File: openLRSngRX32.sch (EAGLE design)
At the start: 50 parts, among them IC1 STM32F10XCXT6, IC2 REG1117, U1 MPU-6000QFN-24

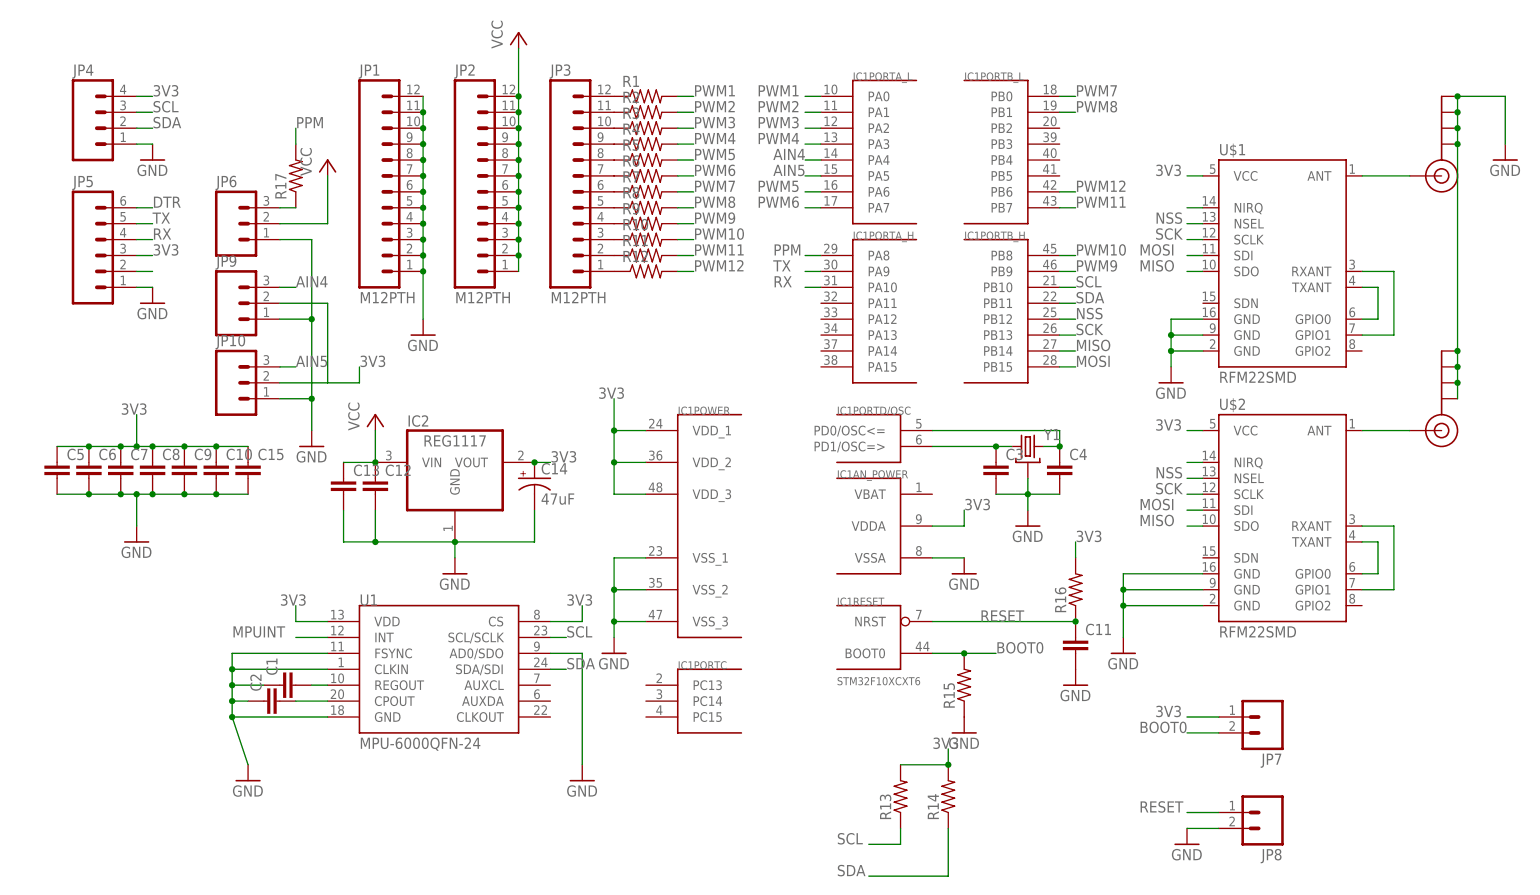
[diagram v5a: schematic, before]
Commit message: more cs lines
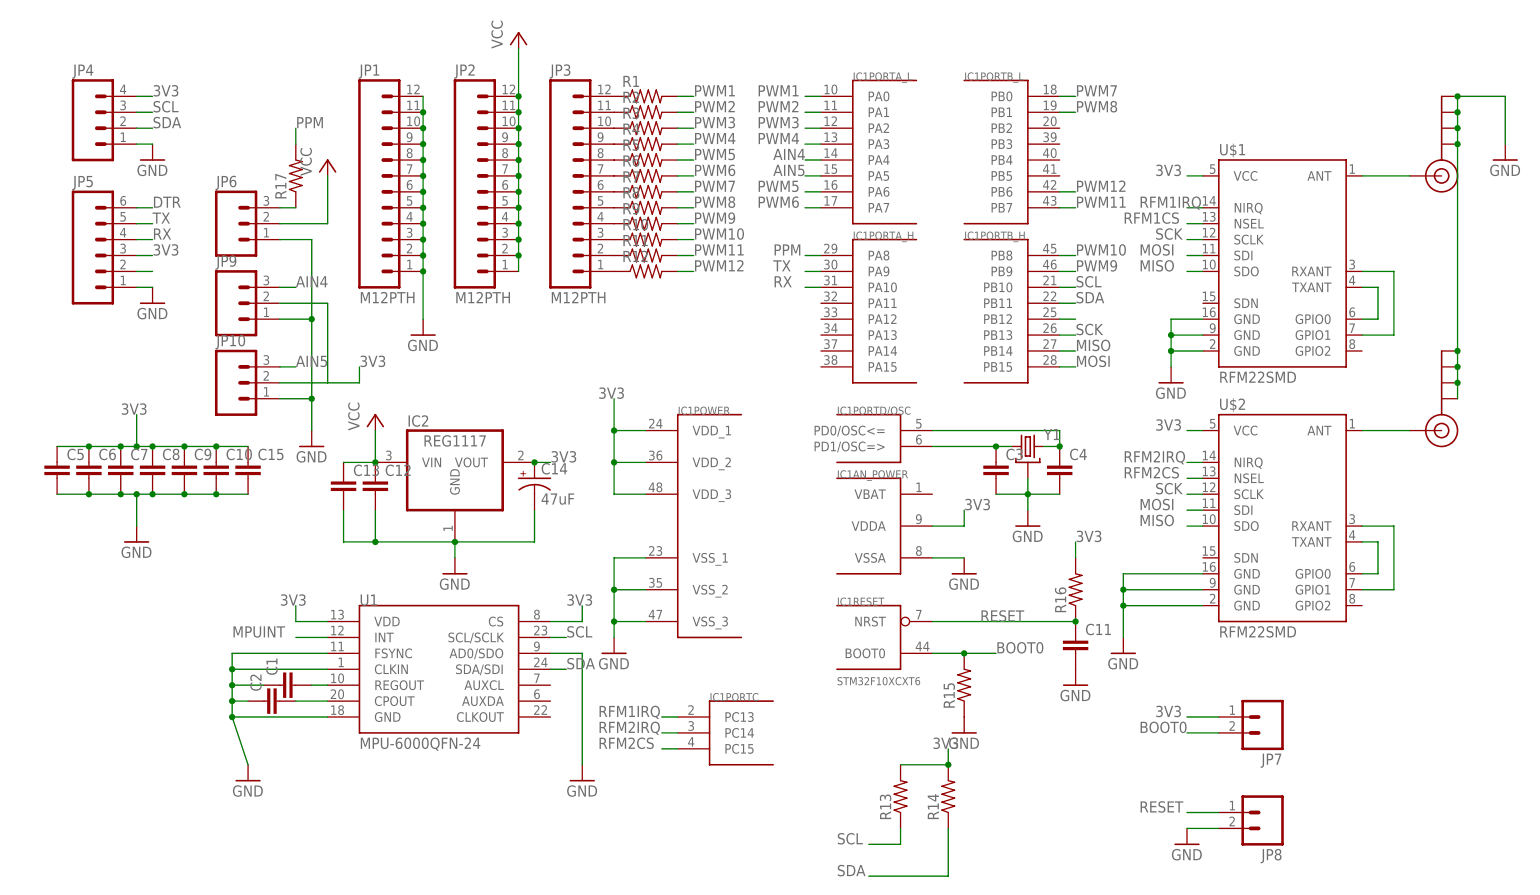
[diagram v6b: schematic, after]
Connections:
- removed net N$21: U$1.NIRQ
- removed net N$22: U$2.NIRQ
- removed net NSS: IC1PORTB_H.PB12, U$1.NSEL, U$2.NSEL
- new net RFM1CS: IC1PORTB_H.PB12, U$1.NSEL
- new net RFM1IRQ: IC1PORTC.PC13, U$1.NIRQ
- new net RFM2CS: IC1PORTC.PC15, U$2.NSEL
- new net RFM2IRQ: IC1PORTC.PC14, U$2.NIRQ
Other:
- moved on the sheet: IC1PORTC
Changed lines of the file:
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@@
 <instance part="IC1" gate="PORTB_H" x="76.2" y="60.96"/>
 <instance part="IC1" gate="POWER" x="30.48" y="25.4"/>
-<instance part="IC1" gate="PORTC" x="27.94" y="-2.54"/>
+<instance part="IC1" gate="PORTC" x="33.02" y="-7.62"/>
 <instance part="IC1" gate="PORTD/OSC" x="58.42" y="40.64"/>
 <instance part="IC1" gate="AN_POWER" x="55.88" y="25.4"/>
@@
 </segment>
 </net>
-<net name="NSS" class="0">
-<segment>
-<pinref part="U$1" gate="G$1" pin="NSEL"/>
-<wire x1="109.22" y1="73.66" x2="106.68" y2="73.66" width="0.1524" layer="91"/>
-<label x="101.6" y="73.66" size="1.778" layer="95"/>
-</segment>
-<segment>
-<pinref part="U$2" gate="G$1" pin="NSEL"/>
-<wire x1="109.22" y1="33.02" x2="106.68" y2="33.02" width="0.1524" layer="91"/>
-<label x="101.6" y="33.02" size="1.778" layer="95"/>
-</segment>
-<segment>
-<pinref part="IC1" gate="PORTB_H" pin="PB12"/>
-<wire x1="86.36" y1="58.42" x2="88.9" y2="58.42" width="0.1524" layer="91"/>
-<label x="88.9" y="58.42" size="1.778" layer="95"/>
-</segment>
-</net>
 <net name="SCK" class="0">
 <segment>
@@
 </segment>
 </net>
-<net name="N$21" class="0">
+<net name="RFM1IRQ" class="0">
 <segment>
 <pinref part="U$1" gate="G$1" pin="NIRQ"/>
 <wire x1="109.22" y1="76.2" x2="106.68" y2="76.2" width="0.1524" layer="91"/>
-</segment>
-</net>
-<net name="N$22" class="0">
+<label x="99.06" y="76.2" size="1.778" layer="95"/>
+</segment>
+<segment>
+<pinref part="IC1" gate="PORTC" pin="PC13"/>
+<wire x1="25.4" y1="-5.08" x2="22.86" y2="-5.08" width="0.1524" layer="91"/>
+<label x="12.7" y="-5.08" size="1.778" layer="95"/>
+</segment>
+</net>
+<net name="RFM2IRQ" class="0">
 <segment>
 <pinref part="U$2" gate="G$1" pin="NIRQ"/>
 <wire x1="109.22" y1="35.56" x2="106.68" y2="35.56" width="0.1524" layer="91"/>
+<label x="96.52" y="35.56" size="1.778" layer="95"/>
+</segment>
+<segment>
+<pinref part="IC1" gate="PORTC" pin="PC14"/>
+<wire x1="25.4" y1="-7.62" x2="22.86" y2="-7.62" width="0.1524" layer="91"/>
+<label x="12.7" y="-7.62" size="1.778" layer="95"/>
 </segment>
 </net>
@@
 </segment>
 </net>
+<net name="RFM2CS" class="0">
+<segment>
+<pinref part="IC1" gate="PORTC" pin="PC15"/>
+<wire x1="25.4" y1="-10.16" x2="22.86" y2="-10.16" width="0.1524" layer="91"/>
+<label x="12.7" y="-10.16" size="1.778" layer="95"/>
+</segment>
+<segment>
+<pinref part="U$2" gate="G$1" pin="NSEL"/>
+<wire x1="109.22" y1="33.02" x2="106.68" y2="33.02" width="0.1524" layer="91"/>
+<label x="96.52" y="33.02" size="1.778" layer="95"/>
+</segment>
+</net>
+<net name="RFM1CS" class="0">
+<segment>
+<pinref part="U$1" gate="G$1" pin="NSEL"/>
+<wire x1="109.22" y1="73.66" x2="106.68" y2="73.66" width="0.1524" layer="91"/>
+<label x="96.52" y="73.66" size="1.778" layer="95"/>
+</segment>
+<segment>
+<pinref part="IC1" gate="PORTB_H" pin="PB12"/>
+<wire x1="86.36" y1="58.42" x2="88.9" y2="58.42" width="0.1524" layer="91"/>
+</segment>
+</net>

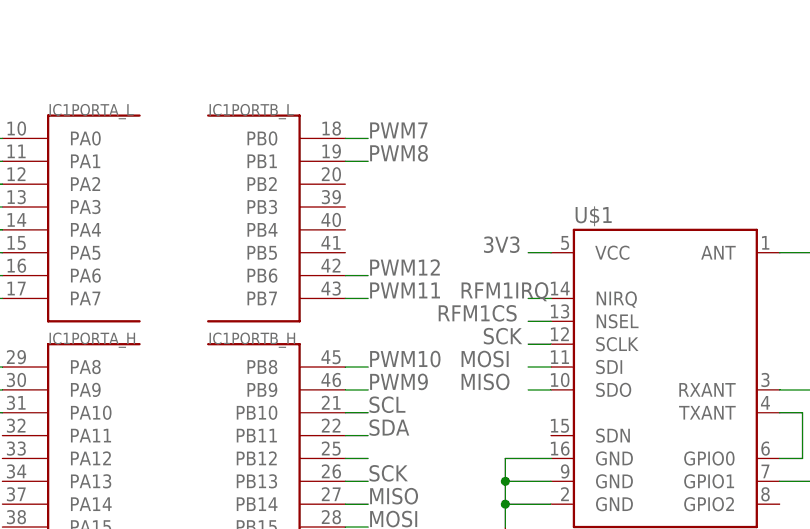
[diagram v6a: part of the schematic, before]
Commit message: MPU interrupt GND reinforcement
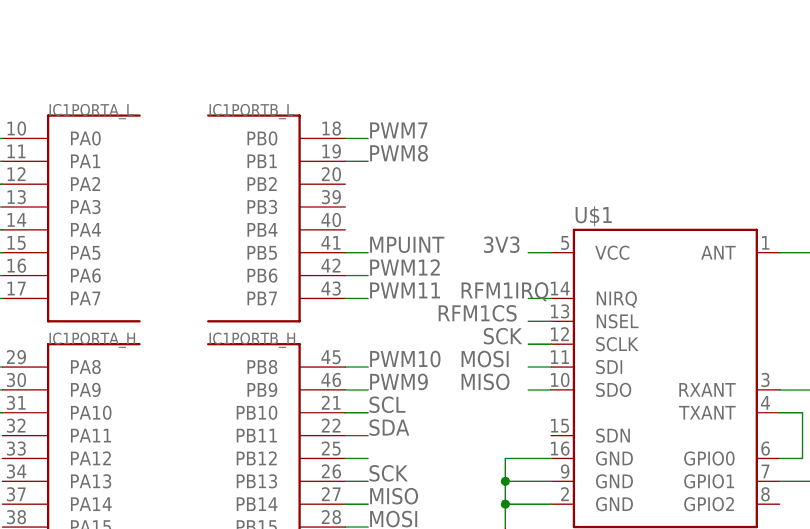
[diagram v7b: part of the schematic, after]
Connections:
- net MPUINT: now also IC1PORTB_L.PB5
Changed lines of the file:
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@@
 <label x="-45.72" y="7.62" size="1.778" layer="95"/>
+</segment>
+<segment>
+<pinref part="IC1" gate="PORTB_L" pin="PB5"/>
+<wire x1="86.36" y1="81.28" x2="88.9" y2="81.28" width="0.1524" layer="91"/>
+<label x="88.9" y="81.28" size="1.778" layer="95"/>
 </segment>
 </net>

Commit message: Last fixes... I hope
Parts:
- added C16: 47uF, SparkFun-Capacitors:47UF-TANT
- added C17: (no value), SparkFun-Capacitors:CAP0805
- added D1: (no value), diode:DIODE-DO-214AC
- added JP11: (no value), SparkFun-Connectors:M02PTH
- added LED1, LED2: (no value), led:LEDSML0805
- added R18, R19: 330R, SparkFun-Resistors:RESISTOR0805-RES
- C1, C13: value (none) -> 100n
- C12: value (none) -> 1uF
- C2: value (none) -> 2n2
- C3, C4: value (none) -> 15p
- R1, R10, R11, R12, R15, R17, R2, R3, R4, R5, R6, R7, R8, R9: value (none) -> 1k
- R13, R14: value (none) -> 4k7
- R16: value (none) -> 10k
- Y1: value (none) -> 8MHz
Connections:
- removed net DTR: JP5.6
- new net N$28: C12.1, C13.1, C16.+, D1.C, IC2.VIN, JP11.2
- new net N$30: LED2.C, R19.2
- new net N$31: IC1PORTA_H.PA11, LED1.A
- new net N$32: IC1PORTA_H.PA14, LED2.A
- net 3V3: now also C17.1, IC1AN_POWER.VBAT
- net GND: now also C16.-, C17.2, JP11.1, R18.1, R19.1, U$1.SDN, U$2.SDN
- net N$29: now also LED1.C, R18.2; no longer JP5.2
- net VCC: now also D1.A; no longer C12.1, C13.1, IC2.VIN
